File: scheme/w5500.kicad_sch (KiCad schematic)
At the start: 51 parts, among them J4 RJ45_Hanrun_HR911105A_Horizon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, U4 W5500, Y2 25Mhz

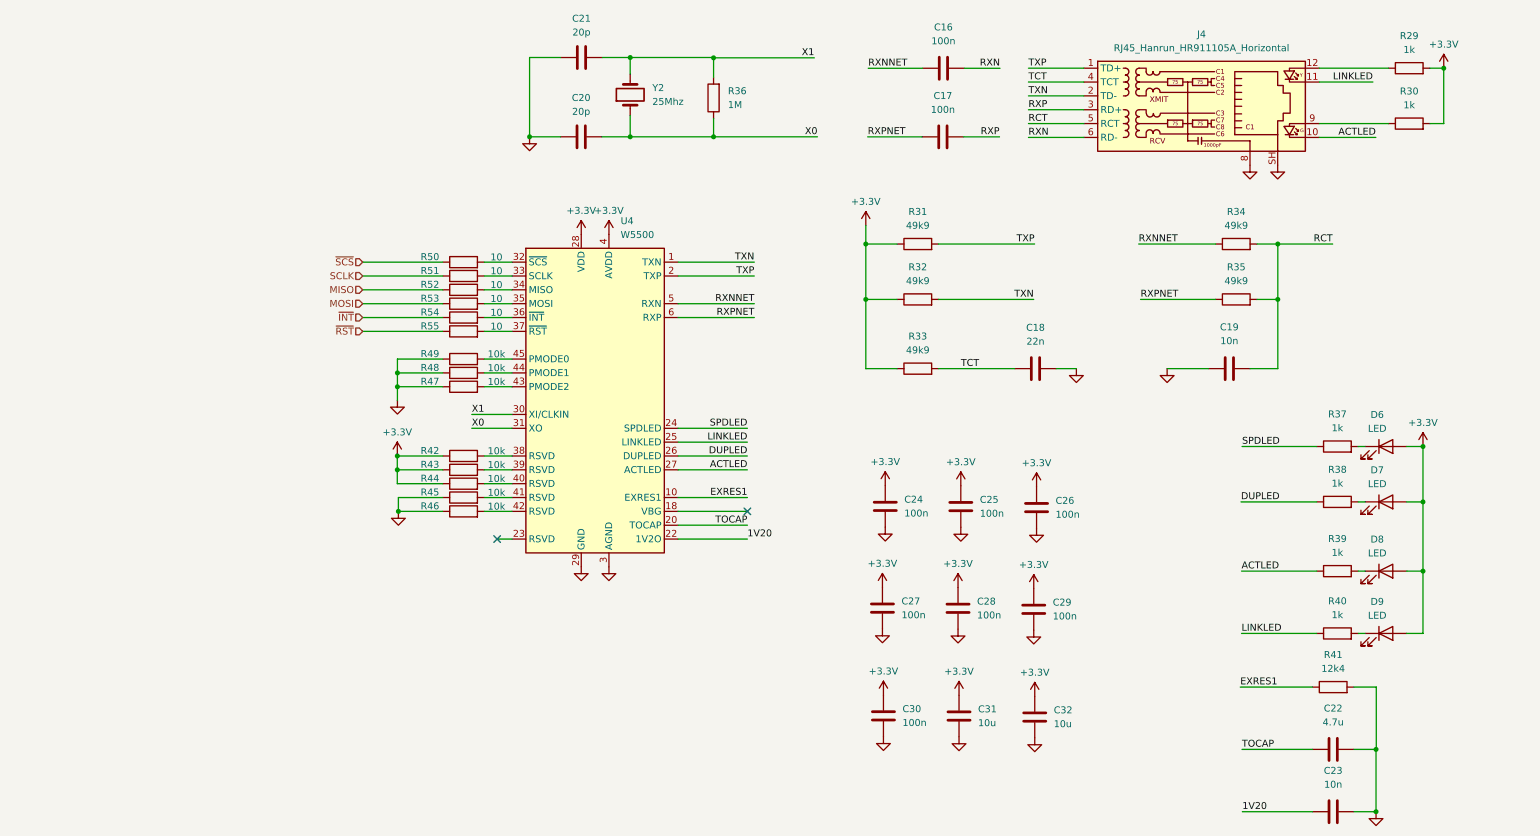
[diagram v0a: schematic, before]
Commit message: feat(schematic): fix peripheral sheets and integrate STM32G0B1CCT6
Главный МК заменён на STM32G0B1CCT6 (LQFP-48, pin-to-pin совместим
с STM32G071CBT6). Лист cpu переписан: обвязка по DS13560, LSE
32.768 кГц, подстроечник на ADC (PA4), перемычка JP_IDD, таблица
назначения выводов.

Исправлены листы периферии:
- st_link: перепутанные USB D+/D-, закороченные резисторы SWD,
  VBUS через PTC и Шоттки, ESD USBLC6-2SC6, LDO AP7361C-33E,
  SWO стянут на землю, J2 1x5 с NRST, перемычка JP_STL_PWR;
- ft232rl: 3V3OUT отвязан от общей шины +3.3V, разделены цепи
  TX/RX и светодиодов, ESD, Шоттки на VBUS, делитель на RESET#;
- w5500: номиналы терминации MDI (49.9 Ом / 10 Ом), PMODE=111,
  RSVD на GND, бусина аналогового питания, подтяжки RST/SCS/INT;
- w32: флэш W25Q32JVSSIQ, символ microSD с детектом карты,
  подтяжки линий SD;
- tmp10x: подтяжки I2C, адреса без резисторов, развязка 100 нФ.

Добавлен лист headers: разъёмы Arduino Uno R3 без ICSP, гребёнки
логического анализатора 1x27 с двух сторон, перемычки JP_SWD.
Удалён пустой лист memory. ERC: 0 ошибок.
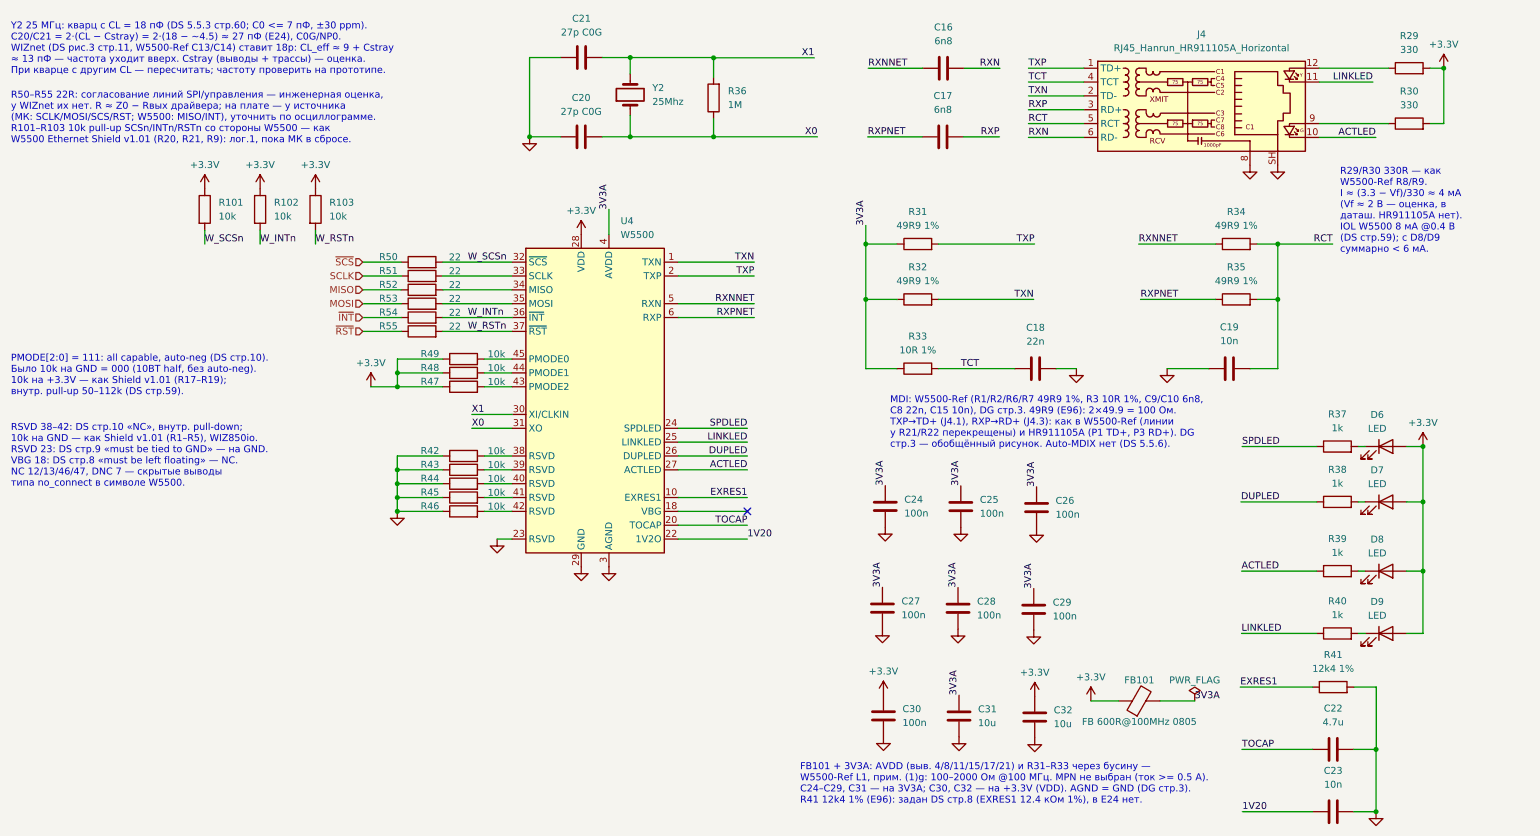
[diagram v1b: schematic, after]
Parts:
- added FB101: FB 600R@100MHz 0805, Inductor_SMD:L_0805_2012Metric, symbol Device:FerriteBead
- added R101, R102, R103: 10k, Resistor_SMD:R_0805_2012Metric, symbol Device:R
- C16, C17: value 100n -> 6n8; footprint (none) -> Capacitor_SMD:C_0805_2012Metric
- C18, C19, C22, C23, C24, C25, C26, C27, C28, C29, C30, C31, C32: footprint (none) -> Capacitor_SMD:C_0805_2012Metric
- C20, C21: value 20p -> 27p C0G; footprint (none) -> Capacitor_SMD:C_0805_2012Metric
- D6, D7, D8, D9: footprint (none) -> LED_SMD:LED_0805_2012Metric
- R29, R30: value 1k -> 330; footprint (none) -> Resistor_SMD:R_0805_2012Metric
- R31, R32, R34, R35: value 49k9 -> 49R9 1%; footprint (none) -> Resistor_SMD:R_0805_2012Metric
- R33: value 49k9 -> 10R 1%; footprint (none) -> Resistor_SMD:R_0805_2012Metric
- R36, R37, R38, R39, R40, R42, R43, R44, R45, R46, R47, R48, R49: footprint (none) -> Resistor_SMD:R_0805_2012Metric
- R41: value 12k4 -> 12k4 1%; footprint (none) -> Resistor_SMD:R_0805_2012Metric
- R50, R51, R52, R53, R54, R55: value 10 -> 22; footprint (none) -> Resistor_SMD:R_0805_2012Metric
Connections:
- net +3.3V: now also R47.1, R48.1, R49.1, FB101.1, R101.1, R102.1, R103.1; no longer C24.1, C25.1, C26.1, C27.1, C28.1, C29.1, C31.1, R31.1, R32.1, R33.1, R42.1, R43.1, R44.1, U4.11 (AVDD), U4.15 (AVDD), U4.17 (AVDD), U4.21 (AVDD), U4.4 (AVDD), U4.8 (AVDD)
- net GND: now also R42.1, R43.1, R44.1, U4.23 (RSVD); no longer R47.1, R48.1, R49.1
- net W_SCSn: now reaches R50.2, U4.32 (~{SCS})
- net W_SCSn: now also R101.2
- net W_INTn: now reaches R54.2, U4.36 (~{INT})
- net W_INTn: now also R102.2
- net W_RSTn: now reaches R55.2, U4.37 (~{RST})
- net W_RSTn: now also R103.2
- new net 3V3A: C24.1, C25.1, C26.1, C27.1, C28.1, C29.1, C31.1, FB101.2, R31.1, R32.1, R33.1, U4.11 (AVDD), U4.15 (AVDD), U4.17 (AVDD), U4.21 (AVDD), U4.4 (AVDD), U4.8 (AVDD)
- no-connect marks 2 -> 1
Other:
- note added: "FB101 + 3V3A: AVDD (выв. 4/8/11/15/17/21) и R31–R33 через бусину — W5500-Ref L1, прим. (1)g: 100–2000 Ом @100 МГц. MPN не выбран (ток >= 0.5 А). C24–C29, C31 — на 3V3A; C30, C32 — на +3.3V (VDD). AGND = GND (DG стр.3). R41 12k4 1% (E96): задан DS стр.8 (EXRES1 12.4 кОм 1%), в E24 нет."
- note added: "MDI: W5500-Ref (R1/R2/R6/R7 49R9 1%, R3 10R 1%, C9/C10 6n8, C8 22n, C15 10n), DG стр.3. 49R9 (E96): 2×49.9 = 100 Ом. TXP→TD+ (J4.1), RXP→RD+ (J4.3): как в W5500-Ref (линии у R21/R22 перекрещены) и HR911105A (P1 TD+, P3 RD+). DG стр.3 — обобщённый рисунок. Auto-MDIX нет (DS 5.5.6)."
- note added: "PMODE[2:0] = 111: all capable, auto-neg (DS стр.10). Было 10k на GND = 000 (10BT half, без auto-neg). 10k на +3.3V — как Shield v1.01 (R17–R19); внутр. pull-up 50–112k (DS стр.59)."
- note added: "R29/R30 330R — как W5500-Ref R8/R9. I ≈ (3.3 − Vf)/330 ≈ 4 мА (Vf ≈ 2 В — оценка, в даташ. HR911105A нет). IOL W5500 8 мА @0.4 В (DS стр.59); с D8/D9 суммарно < 6 мА."
- note added: "R50–R55 22R: согласование линий SPI/управления — инженерная оценка, у WIZnet их нет. R ≈ Z0 − Rвых драйвера; на плате — у источника (МК: SCLK/MOSI/SCS/RST; W5500: MISO/INT), уточнить по осциллограмме. R101–R103 10k pull-up SCSn/INTn/RSTn со стороны W5500 — как W5500 Ethernet Shield v1.01 (R20, R21, R9): лог.1, пока МК в сбросе."
- note added: "RSVD 38–42: DS стр.10 «NC», внутр. pull-down; 10k на GND — как Shield v1.01 (R1–R5), WIZ850io. RSVD 23: DS стр.9 «must be tied to GND» — на GND. VBG 18: DS стр.8 «must be left floating» — NC. NC 12/13/46/47, DNC 7 — скрытые выводы типа no_connect в символе W5500."
- note added: "Y2 25 МГц: кварц с CL = 18 пФ (DS 5.5.3 стр.60; C0 <= 7 пФ, ±30 ppm). C20/C21 = 2·(CL − Cstray) = 2·(18 − ~4.5) ≈ 27 пФ (E24), C0G/NP0. WIZnet (DS рис.3 стр.11, W5500-Ref C13/C14) ставит 18p: CL_eff ≈ 9 + Cstray ≈ 13 пФ — частота уходит вверх. Cstray (выводы + трассы) — оценка. При кварце с другим CL — пересчитать; частоту проверить на прототипе."
- moved on the sheet: R50, R51, R52, R53, R54, R55

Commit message: refactor(schematic): re-annotate references by sheet number
Позиционные обозначения перенумерованы по схеме «номер листа x 100»:
cpu - 1xx, st_link - 2xx, ft232rl - 3xx, w5500 - 4xx, w32 - 5xx,
tmp10x - 6xx, leds - 7xx, headers - 8xx. По обозначению на плате
сразу видно, к какому листу относится компонент.

Ссылки на компоненты в текстовых комментариях обновлены. Обозначения
из сторонних референсных схем (MB1136, MB1184, W5500-Ref, Ethernet
Shield, Adafruit) и имена выводов Arduino оставлены без изменений.

Проверено: нетлист до и после совпадает с точностью до переименования
(190 цепей, 187 компонентов), дубликатов нет, ERC - 0 ошибок.
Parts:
- renumbered C21 to C401, C20 to C402, C24 to C403, C27 to C404, C30 to C405, C16 to C406, C17 to C407, C28 to C408, C31 to C409, C25 to C410, C18 to C411, C26 to C412, C29 to C413, C32 to C414, C19 to C415, C22 to C416, C23 to C417, D6 to D401, D7 to D402, D8 to D403, D9 to D404, FB101 to FB401, J4 to J401, R101 to R401, R102 to R402, R103 to R403, R50 to R404, R51 to R405, R52 to R406, R53 to R407, R54 to R408, R55 to R409, R49 to R410, R48 to R411, R47 to R412, R42 to R413, R43 to R414, R44 to R415, R45 to R416, R46 to R417, R36 to R418, R31 to R419, R32 to R420, R33 to R421, R34 to R422, R35 to R423, R37 to R424, R38 to R425, R39 to R426, R40 to R427, R41 to R428, R29 to R429, R30 to R430, U4 to U401, Y2 to Y401
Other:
- note added: "FB401 + 3V3A: AVDD (выв. 4/8/11/15/17/21) и R419–R421 через бусину — W5500-Ref L1, прим. (1)g: 100–2000 Ом @100 МГц. MPN не выбран (ток >= 0.5 А). C403–C413, C409 — на 3V3A; C405, C414 — на +3.3V (VDD). AGND = GND (DG стр.3). R428 12k4 1% (E96): задан DS стр.8 (EXRES1 12.4 кОм 1%), в E24 нет."
- note added: "MDI: W5500-Ref (R1/R2/R6/R7 49R9 1%, R3 10R 1%, C9/C10 6n8, C8 22n, C15 10n), DG стр.3. 49R9 (E96): 2×49.9 = 100 Ом. TXP→TD+ (J401.1), RXP→RD+ (J401.3): как в W5500-Ref (линии у R21/R22 перекрещены) и HR911105A (P1 TD+, P3 RD+). DG стр.3 — обобщённый рисунок. Auto-MDIX нет (DS 5.5.6)."
- note added: "R404–R409 22R: согласование линий SPI/управления — инженерная оценка, у WIZnet их нет. R ≈ Z0 − Rвых драйвера; на плате — у источника (МК: SCLK/MOSI/SCS/RST; W5500: MISO/INT), уточнить по осциллограмме. R401–R403 10k pull-up SCSn/INTn/RSTn со стороны W5500 — как W5500 Ethernet Shield v1.01 (R20, R21, R9): лог.1, пока МК в сбросе."
- note added: "R429/R430 330R — как W5500-Ref R8/R9. I ≈ (3.3 − Vf)/330 ≈ 4 мА (Vf ≈ 2 В — оценка, в даташ. HR911105A нет). IOL W5500 8 мА @0.4 В (DS стр.59); с D403/D404 суммарно < 6 мА."
- note added: "Y401 25 МГц: кварц с CL = 18 пФ (DS 5.5.3 стр.60; C0 <= 7 пФ, ±30 ppm). C402/C401 = 2·(CL − Cstray) = 2·(18 − ~4.5) ≈ 27 пФ (E24), C0G/NP0. WIZnet (DS рис.3 стр.11, W5500-Ref C13/C14) ставит 18p: CL_eff ≈ 9 + Cstray ≈ 13 пФ — частота уходит вверх. Cstray (выводы + трассы) — оценка. При кварце с другим CL — пересчитать; частоту проверить на прототипе."
- note removed: "FB101 + 3V3A: AVDD (выв. 4/8/11/15/17/21) и R31–R33 через бусину — W5500-Ref L1, прим. (1)g: 100–2000 Ом @100 МГц. MPN не выбран (ток >= 0.5 А). C24–C29, C31 — на 3V3A; C30, C32 — на +3.3V (VDD). AGND = GND (DG стр.3). R41 12k4 1% (E96): задан DS стр.8 (EXRES1 12.4 кОм 1%), в E24 нет."
- note removed: "MDI: W5500-Ref (R1/R2/R6/R7 49R9 1%, R3 10R 1%, C9/C10 6n8, C8 22n, C15 10n), DG стр.3. 49R9 (E96): 2×49.9 = 100 Ом. TXP→TD+ (J4.1), RXP→RD+ (J4.3): как в W5500-Ref (линии у R21/R22 перекрещены) и HR911105A (P1 TD+, P3 RD+). DG стр.3 — обобщённый рисунок. Auto-MDIX нет (DS 5.5.6)."
- note removed: "R29/R30 330R — как W5500-Ref R8/R9. I ≈ (3.3 − Vf)/330 ≈ 4 мА (Vf ≈ 2 В — оценка, в даташ. HR911105A нет). IOL W5500 8 мА @0.4 В (DS стр.59); с D8/D9 суммарно < 6 мА."
- note removed: "R50–R55 22R: согласование линий SPI/управления — инженерная оценка, у WIZnet их нет. R ≈ Z0 − Rвых драйвера; на плате — у источника (МК: SCLK/MOSI/SCS/RST; W5500: MISO/INT), уточнить по осциллограмме. R101–R103 10k pull-up SCSn/INTn/RSTn со стороны W5500 — как W5500 Ethernet Shield v1.01 (R20, R21, R9): лог.1, пока МК в сбросе."
- note removed: "Y2 25 МГц: кварц с CL = 18 пФ (DS 5.5.3 стр.60; C0 <= 7 пФ, ±30 ppm). C20/C21 = 2·(CL − Cstray) = 2·(18 − ~4.5) ≈ 27 пФ (E24), C0G/NP0. WIZnet (DS рис.3 стр.11, W5500-Ref C13/C14) ставит 18p: CL_eff ≈ 9 + Cstray ≈ 13 пФ — частота уходит вверх. Cstray (выводы + трассы) — оценка. При кварце с другим CL — пересчитать; частоту проверить на прототипе."

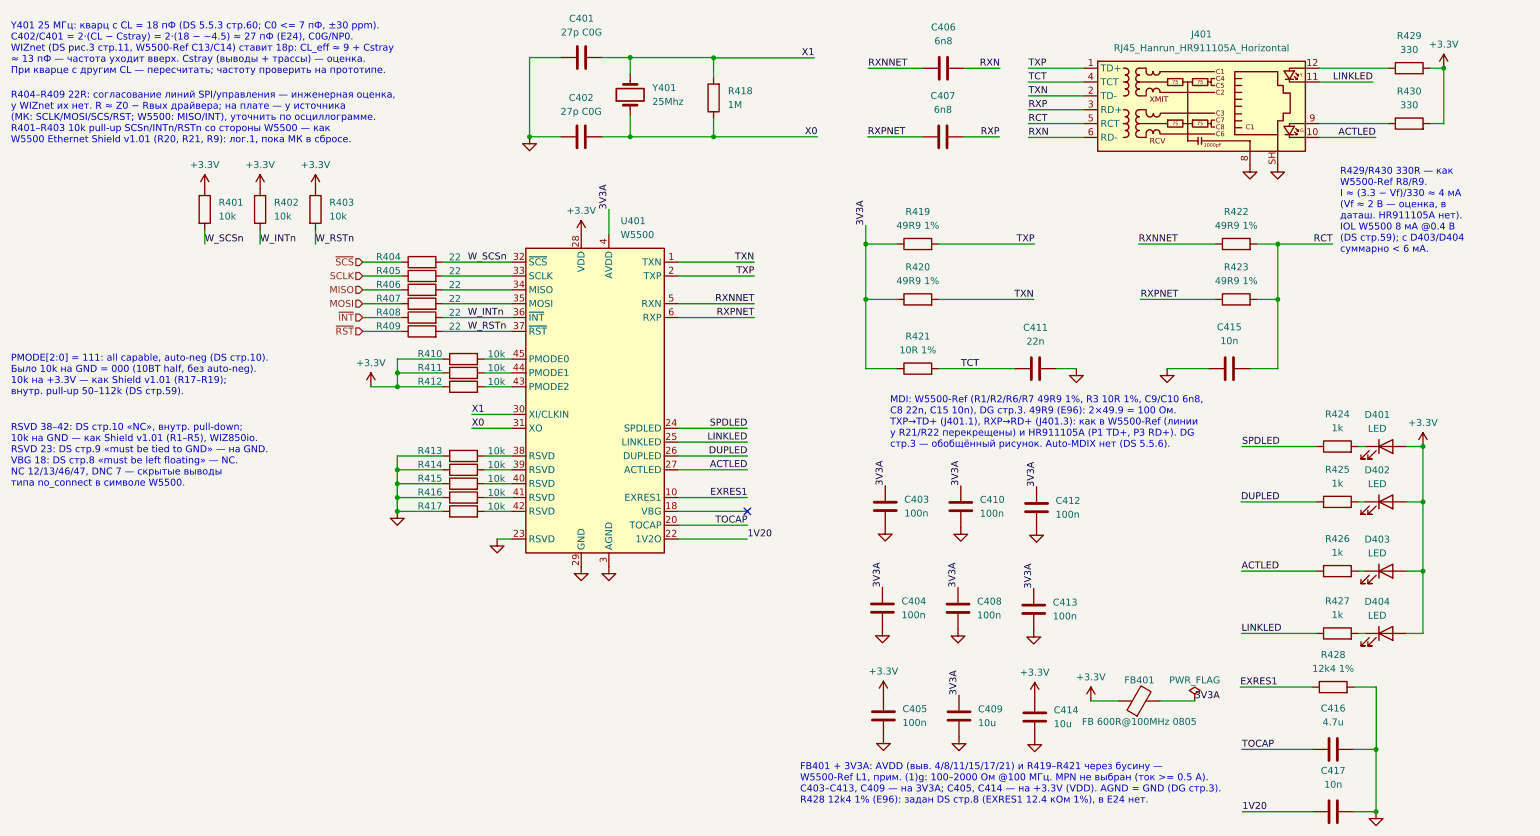
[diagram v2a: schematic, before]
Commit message: fix(schematic): resolve all ERC warnings
ERC: 0 ошибок, 0 предупреждений (было 239 предупреждений).

- w5500, leds: все объекты перенесены на сетку 1.27 мм; удалены
  два провода нулевой длины.
- Заведена проектная библиотека g0_dev_board.kicad_sym (+ sym-lib-table)
  для намеренно изменённых символов: USB_B_Mini с пассивными
  VBUS/GND (J201, J301). Попутно исправлен номер вывода экрана
  6 -> SH: у footprint Lumberg 2486 01 площадки экрана называются SH,
  иначе экран на плате остался бы неподключённым.
- Устаревшие копии символа LED обновлены из стандартной библиотеки.
- Кнопки SW701/SW702: SW_DPST_x2 заменён на SW_Push, footprint
  SW_SPST_PTS645Sx43SMTR92 (площадки 1,1,2,2 уже попарно замкнуты).
- Флэш U501: WP и HOLD подтянуты к +3.3V через R516/R517 10k
  вместо прямого подключения к выходу LDO.

Связность проверена сравнением нетлистов: изменились только цепи
WP/HOLD флэша.
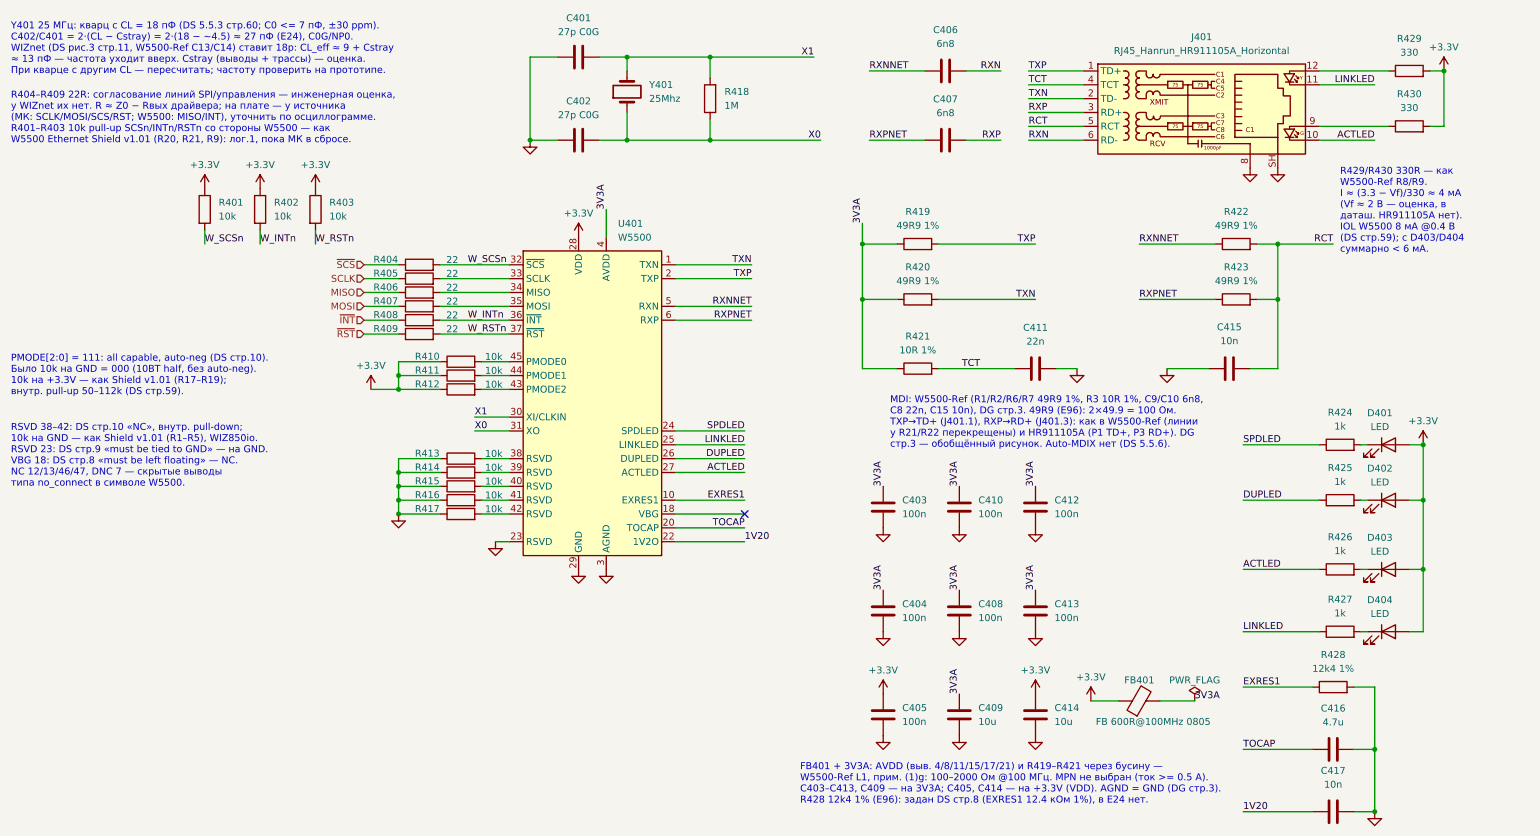
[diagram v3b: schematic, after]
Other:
- moved on the sheet: C401, C402, C404, C406, C407, C408, D401, D402, D403, D404, J401, R404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
